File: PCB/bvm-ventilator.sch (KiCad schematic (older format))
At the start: 3 parts, among them U1 IEC_CONNECTOR

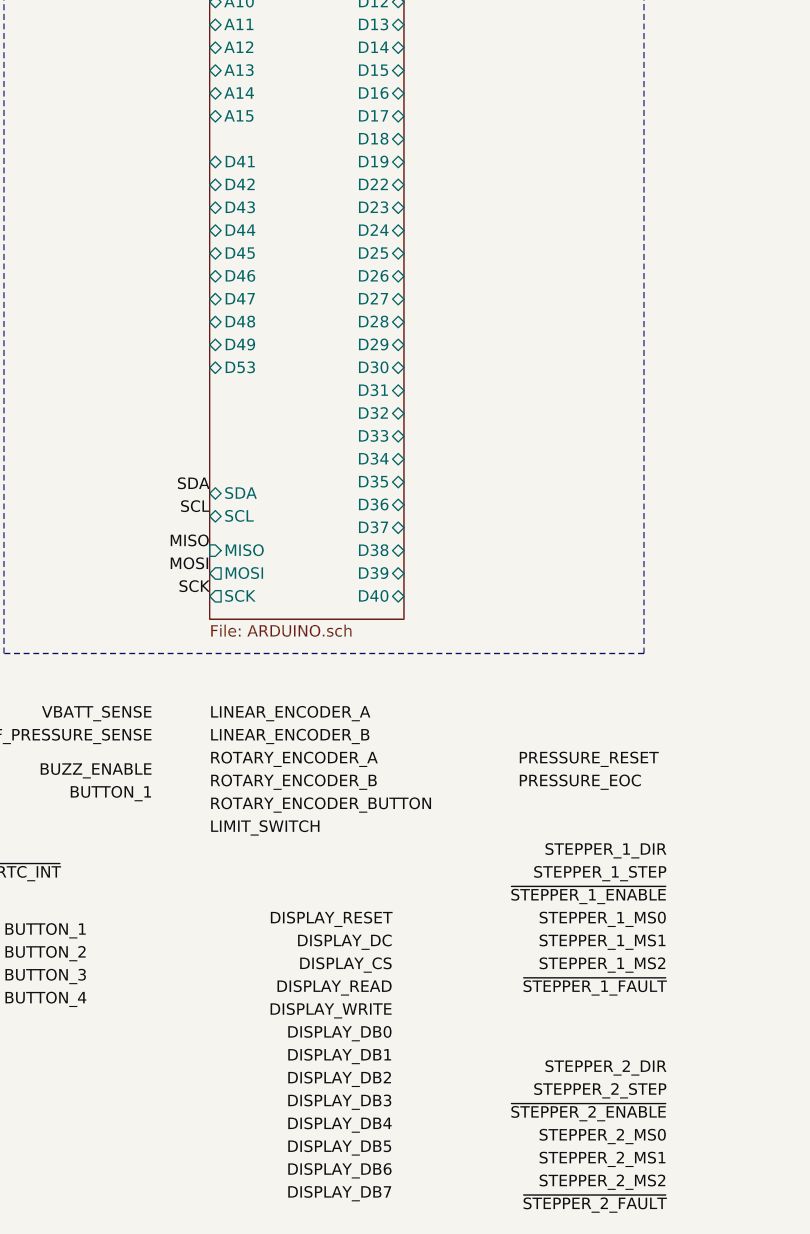
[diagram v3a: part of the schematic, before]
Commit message: Connected Display pins to Mega
They are hardcoded in the library I will use, see:
https://learn.adafruit.com/adafruit-2-4-color-tft-touchscreen-breakout/8-bit-wiring-and-test
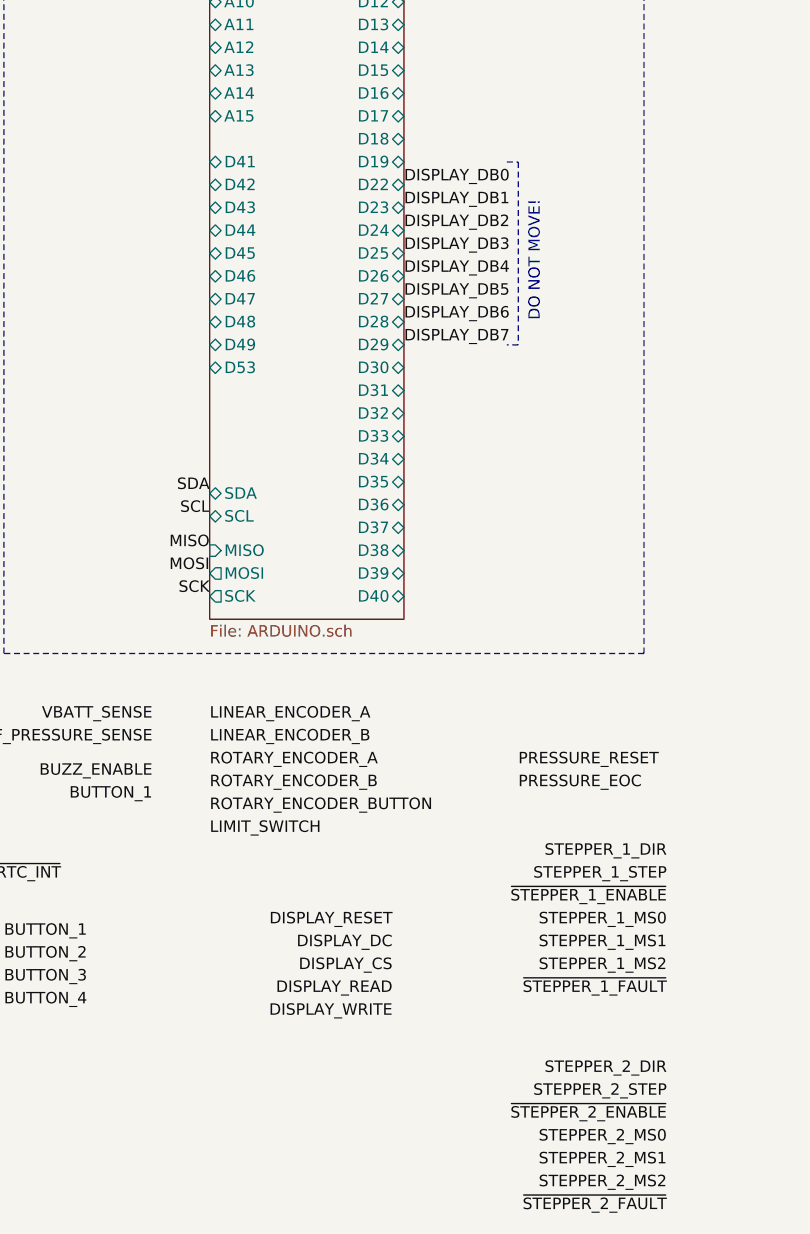
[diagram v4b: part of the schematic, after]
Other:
- note added: "DO NOT MOVE!"
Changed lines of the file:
@@
 Text Label 9800 5600 0    50   ~ 0
 DISPLAY_DB7
-Text Label 2550 6800 2    50   ~ 0
+Text Label 2600 3050 0    50   ~ 0
 DISPLAY_DB0
-Text Label 2550 6900 2    50   ~ 0
+Text Label 2600 3150 0    50   ~ 0
 DISPLAY_DB1
-Text Label 2550 7000 2    50   ~ 0
-DISPLAY_DB2
-Text Label 2550 7100 2    50   ~ 0
+Text Label 2600 3350 0    50   ~ 0
 DISPLAY_DB3
-Text Label 2550 7200 2    50   ~ 0
+Text Label 2600 3450 0    50   ~ 0
 DISPLAY_DB4
-Text Label 2550 7300 2    50   ~ 0
+Text Label 2600 3550 0    50   ~ 0
 DISPLAY_DB5
-Text Label 2550 7400 2    50   ~ 0
+Text Label 2600 3650 0    50   ~ 0
 DISPLAY_DB6
-Text Label 2550 7500 2    50   ~ 0
+Text Label 2600 3750 0    50   ~ 0
 DISPLAY_DB7
 Wire Notes Line
 	10350 5850 10350 3350
+Text Label 2600 3250 0    50   ~ 0
+DISPLAY_DB2
+Wire Notes Line
+	3050 2950 3100 2950
+Wire Notes Line
+	3100 2950 3100 3750
+Wire Notes Line
+	3100 3750 3050 3750
+Text Notes 3200 3650 1    50   ~ 0
+DO NOT MOVE!
 $EndSCHEMATC

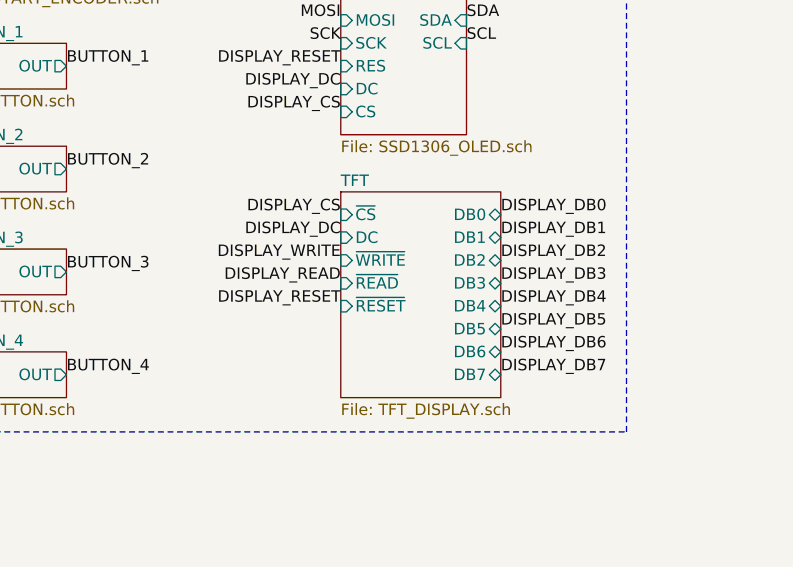
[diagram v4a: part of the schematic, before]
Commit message: Renamed TFT interface pins
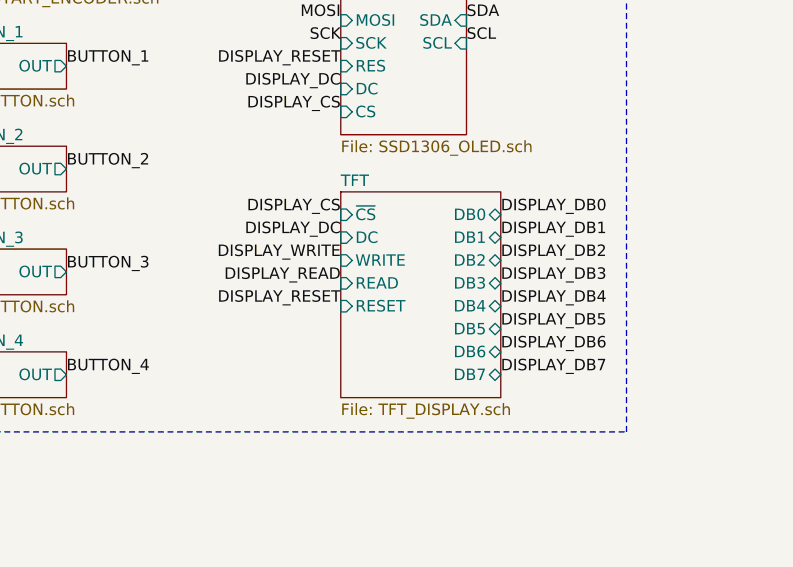
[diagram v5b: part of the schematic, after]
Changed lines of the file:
@@
 Text Label 9100 4250 2    50   ~ 0
 DISPLAY_RESET
-$Sheet
-S 9100 4800 700  900
-U 5E97D98A
-F0 "TFT" 50
-F1 "TFT_DISPLAY.sch" 50
-F2 "~CS" I L 9100 4900 50
-F3 "DC" I L 9100 5000 50
-F4 "~WRITE" I L 9100 5100 50
-F5 "~READ" I L 9100 5200 50
-F6 "~RESET" I L 9100 5300 50
-F7 "DB0" B R 9800 4900 50
-F8 "DB1" B R 9800 5000 50
-F9 "DB2" B R 9800 5100 50
-F10 "DB3" B R 9800 5200 50
-F11 "DB4" B R 9800 5300 50
-F12 "DB5" B R 9800 5400 50
-F13 "DB6" B R 9800 5500 50
-F14 "DB7" B R 9800 5600 50
-$EndSheet
 Text Label 2550 6300 2    50   ~ 0
 DISPLAY_RESET
@@
 Text Notes 3200 3650 1    50   ~ 0
 DO NOT MOVE!
+$Sheet
+S 9100 4800 700  900
+U 5E97D98A
+F0 "TFT" 50
+F1 "TFT_DISPLAY.sch" 50
+F2 "~CS" I L 9100 4900 50
+F3 "DC" I L 9100 5000 50
+F4 "DB0" B R 9800 4900 50
+F5 "DB1" B R 9800 5000 50
+F6 "DB2" B R 9800 5100 50
+F7 "DB3" B R 9800 5200 50
+F8 "DB4" B R 9800 5300 50
+F9 "DB5" B R 9800 5400 50
+F10 "DB6" B R 9800 5500 50
+F11 "DB7" B R 9800 5600 50
+F12 "WRITE" I L 9100 5100 50
+F13 "READ" I L 9100 5200 50
+F14 "RESET" I L 9100 5300 50
+$EndSheet
 $EndSCHEMATC

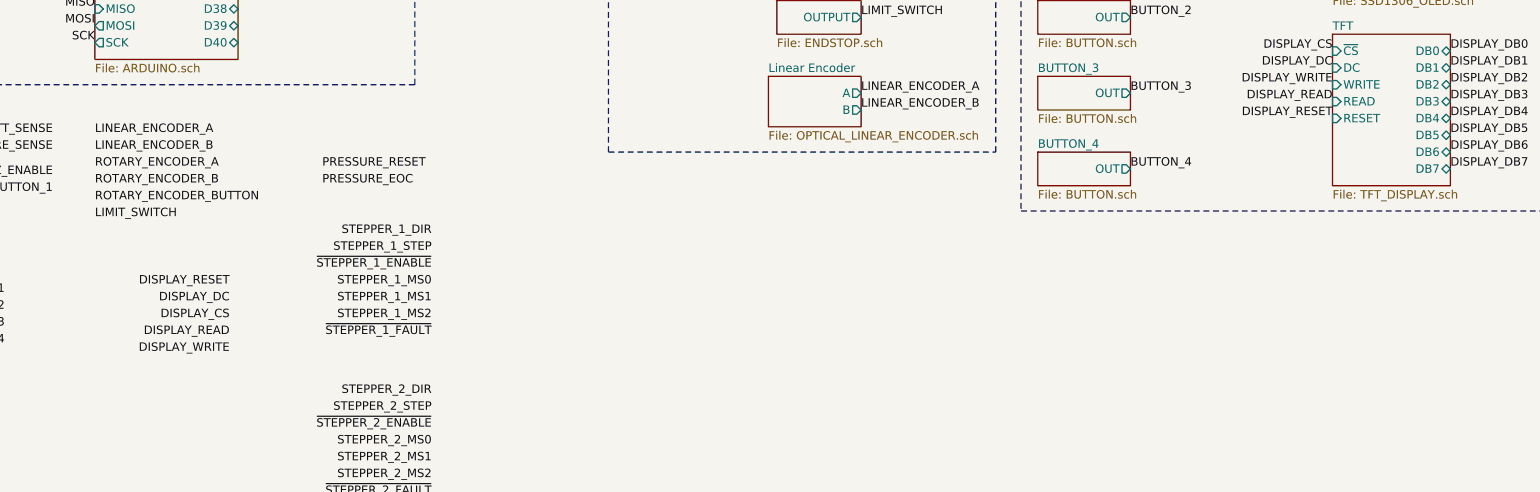
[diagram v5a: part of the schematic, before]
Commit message: Added decoupling and voltage regulation
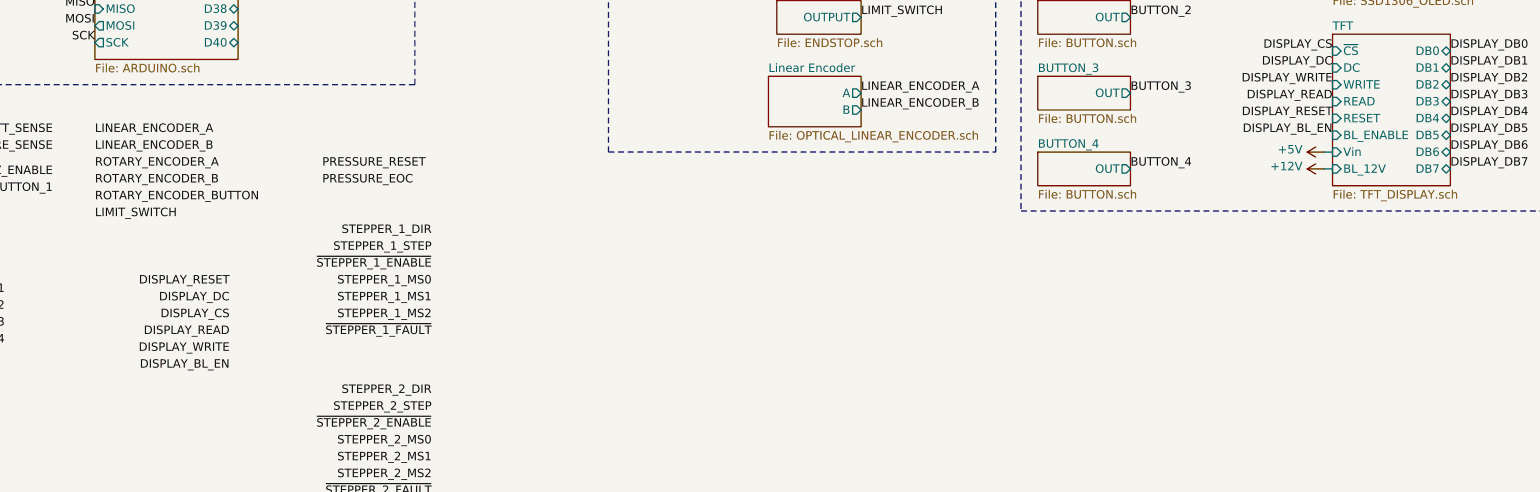
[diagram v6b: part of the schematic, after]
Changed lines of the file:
@@
 $Descr A4 11693 8268
 encoding utf-8
-Sheet 1 27
+Sheet 1 28
 Title "ResQVenT"
 Date ""
@@
 F13 "READ" I L 9100 5200 50
 F14 "RESET" I L 9100 5300 50
-$EndSheet
+F15 "BL_ENABLE" I L 9100 5400 50
+F16 "BL_12V" I L 9100 5600 50
+F17 "Vin" I L 9100 5500 50
+$EndSheet
+Text Label 9100 5400 2    50   ~ 0
+DISPLAY_BL_EN
+Text Label 2550 6800 2    50   ~ 0
+DISPLAY_BL_EN
+$Comp
+L power:+12V #PWR0182
+U 1 1 5EA9BDF2
+P 9050 5600
+F 0 "#PWR0182" H 9050 5450 50  0001 C CNN
+F 1 "+12V" V 9065 5728 50  0000 L CNN
+F 2 "" H 9050 5600 50  0001 C CNN
+F 3 "" H 9050 5600 50  0001 C CNN
+	1    9050 5600
+	0    -1   -1   0
+$EndComp
+Wire Wire Line
+	9050 5600 9100 5600
+$Comp
+L power:+5V #PWR?
+U 1 1 5EAD492F
+P 9050 5500
+F 0 "#PWR?" H 9050 5350 50  0001 C CNN
+F 1 "+5V" V 9065 5628 50  0000 L CNN
+F 2 "" H 9050 5500 50  0001 C CNN
+F 3 "" H 9050 5500 50  0001 C CNN
+	1    9050 5500
+	0    -1   -1   0
+$EndComp
+Wire Wire Line
+	9050 5500 9100 5500
 $EndSCHEMATC
